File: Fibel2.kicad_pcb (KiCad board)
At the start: 4 copper layers, 210 x 148 mm, 476 parts, among them IC1 ICS-43434, IC2 ICS-43434, IC3 ICS-43434, IC4 ICS-43434, IC5 TXB0108RGYR, IC6 TXB0108RGYR, IC7 TXB0108RGYR, IC8 TS3A27518ERTWR, IC9 TXB0108RGYR, J1 Raspi_Header, J10 Conn_01x04, J11 Conn_01x05, J1201 Orin Nano, J2 Raspi_Header, J3 Conn_01x02, J301 Conn_01x02, J302 Conn_01x02, J303 Conn_01x02, J4 ED060SC4, J401 USB-C_USB4105-GF-A, J402 Conn_USB-C_WE_632723300011, J5 ED060SC7, J6 DM3AT-SF-PEJM5_40_, J8 SJ2-35954D-SMT-TR, J9 Conn_01x02, J901 Bus_M.2_2199230-6, J902 Bus_M.2_1-2199230-6, Q1 PJE138K_2, Q2 PJE138K_2, Q301 CSD17581Q3A, Q302 CSD17581Q3A, Q303 CSD17581Q3A, Q304 CSD17581Q3A, U1 TPS651851RSLT, U2 74LVC2G14_SOT457, U202 TLV75733PDBV, U204 TPS56428DDA, U205 TPS56428DDA, U3 TPS65988DHRSHR, U301 BQ25798RQMR, U4 ESP32-S3-WROOM-1U, U403 FT230X_QFN, U404 AP22615_1, U405 TUSB1046-DCIRNQ, U406 AP22615_1, U407 TPD4E05U06QDQARQ1, U408 TPD4E05U06QDQARQ1, U409 W25Q80DV_USON, U410 TPD4E05U06QDQARQ1, U411 TPD4E05U06QDQARQ1, U412 TPD4E05U06QDQARQ1, U5 TLV75733PDBV, U6 74LVC1G175_SOT457, U7 TLV75733PDBV, U701 WM8960CGEFL, U8 PCAL6408A_VQFN, X701 24MHz 306020014, Y1 ECS-327ATQ2520MV-32.786K

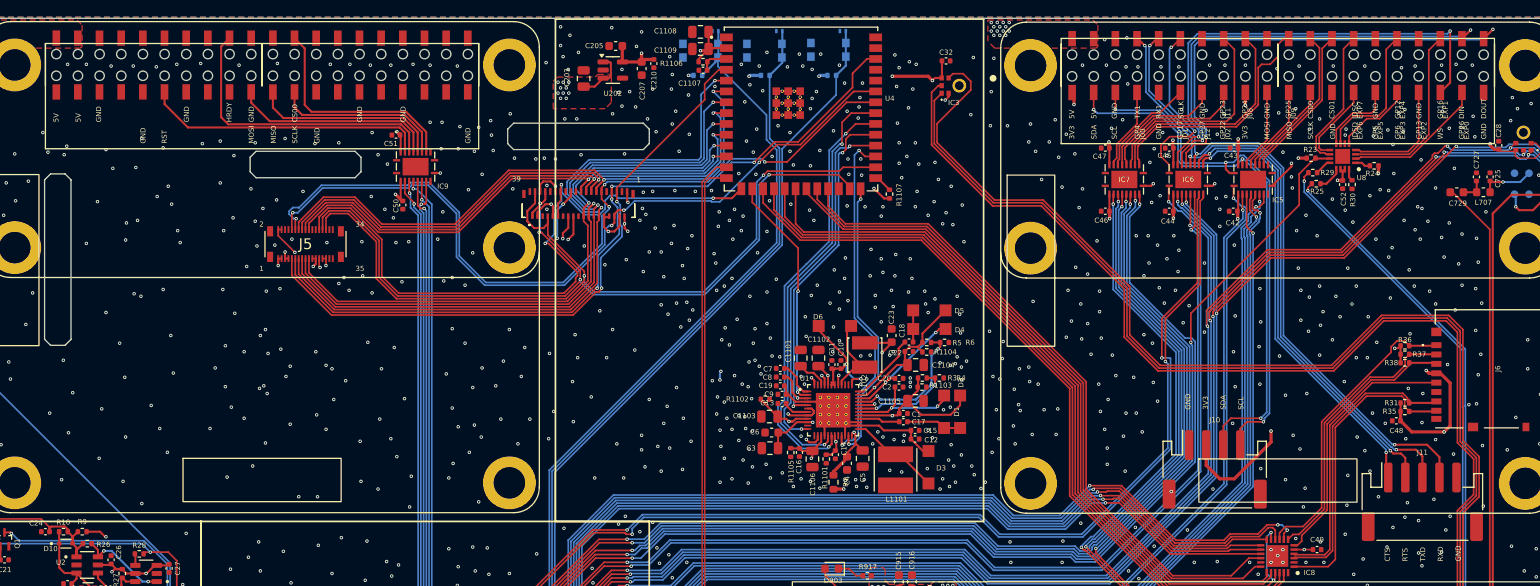
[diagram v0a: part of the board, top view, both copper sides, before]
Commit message: added second i2c, modified 40 pin headers
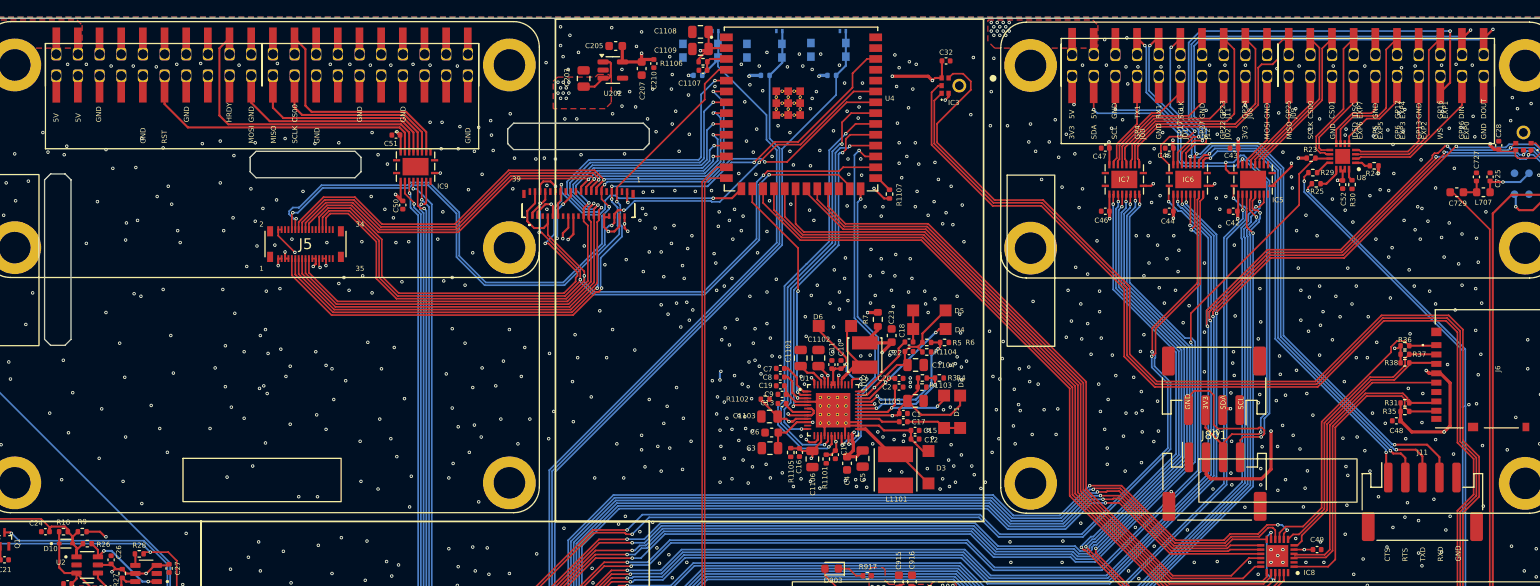
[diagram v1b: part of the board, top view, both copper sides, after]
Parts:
- added J801: Conn_01x04, Connector_JST:JST_PH_S4B-PH-SM4-TB_1x04-1MP_P2.00mm_Horizontal, F.Cu at (181.6, 58.1)
- moved R7 19.8 mm to (142.2, 50.3), turned to 90 degrees
- moved J10 1.43 mm to (181.7, 69.3)
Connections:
- R7 pad 2: +5V -> EPD_3V3
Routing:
- net +5V: track 323.6 -> 305.3 mm, vias 90 -> 89
- net I2C2_SCL_3V: track 61.7 -> 77.5 mm
- net EPD_3V3: track 297.1 -> 306.5 mm, vias 14 -> 15
- net +3V3: track 522.4 -> 531.7 mm, vias 97 -> 98
- net I2C2_SDA_3V: track 64.1 -> 70.3 mm
- net I2S1_SCLK: track 324.7 -> 327.6 mm
- net I2S1_WS: track 318.4 -> 321.3 mm
- net I2S1_DIN: track 318.7 -> 321.6 mm
- net UART1_CTS: track 193.0 -> 194.4 mm
- net GND: vias 2188 -> 2210
